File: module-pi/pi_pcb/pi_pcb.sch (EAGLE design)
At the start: 14 parts, among them K1 PIN20X2, X1 SSW-114-02-G-S, X2 SSW-114-02-G-S, X3 SSW-114-02-G-S, X4 SSW-114-02-G-S

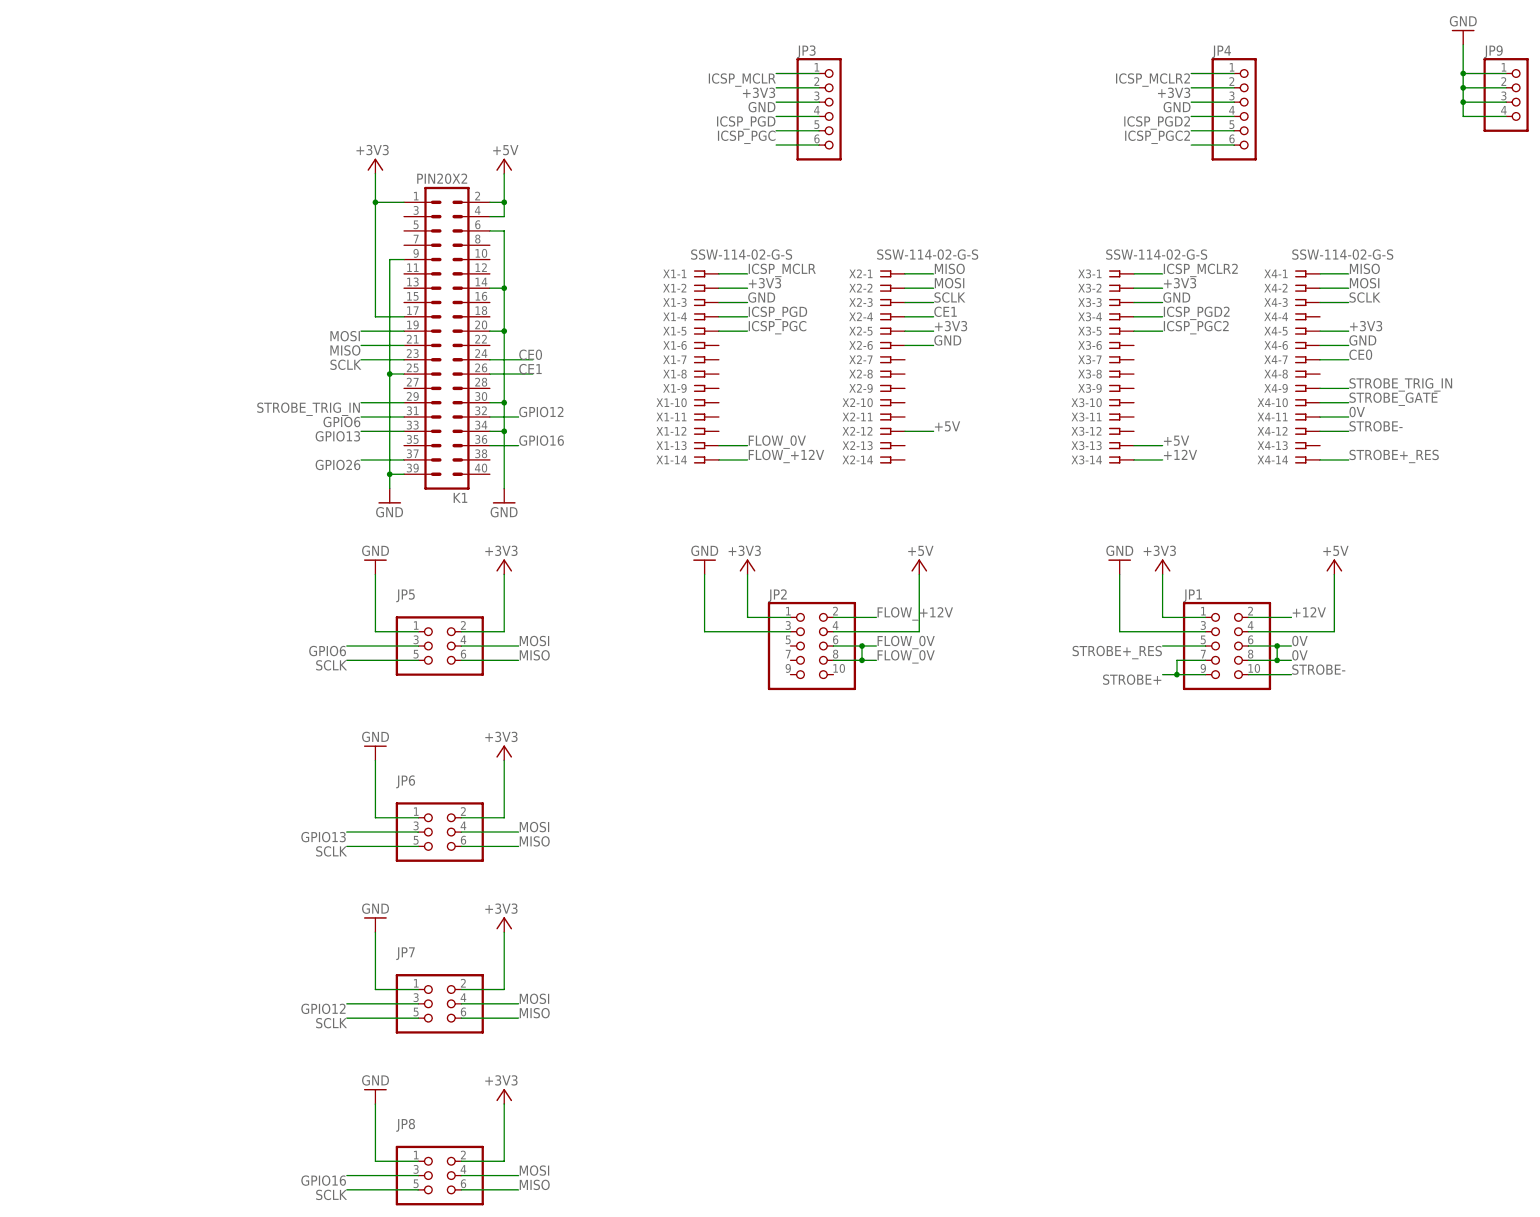
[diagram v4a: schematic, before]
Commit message: External strobe trigger added.  Text and boxes added.
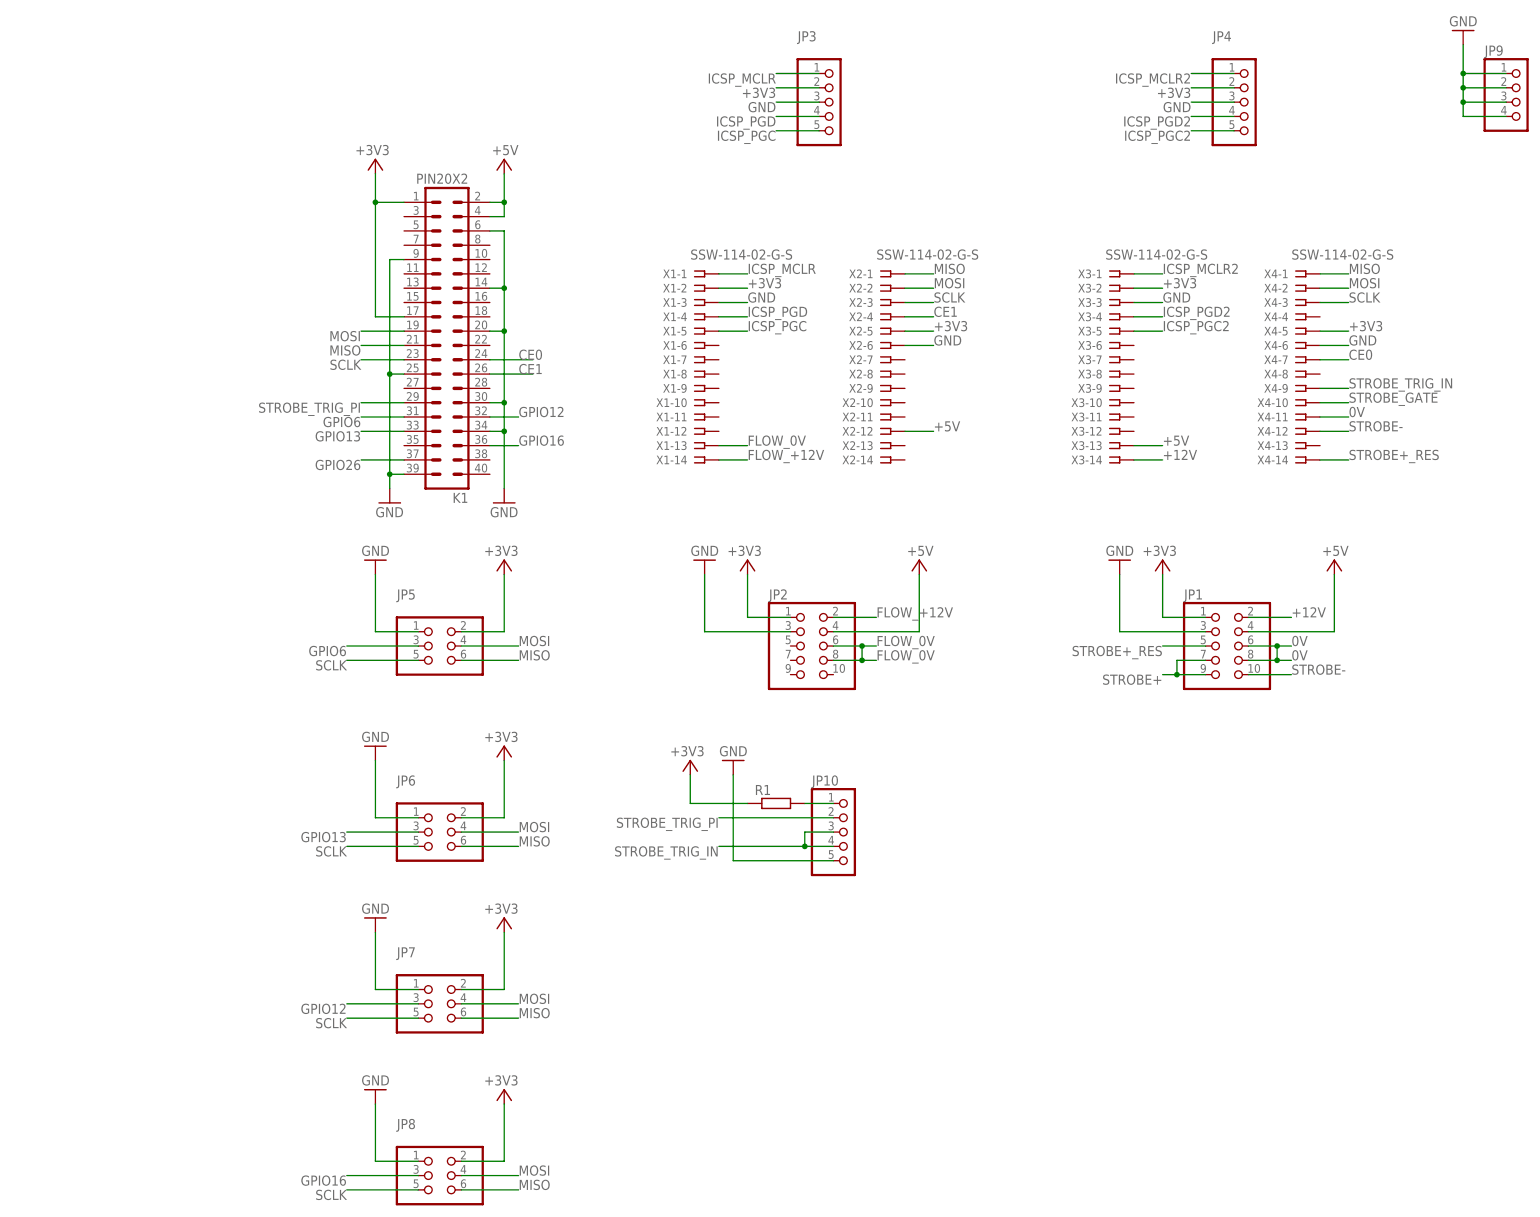
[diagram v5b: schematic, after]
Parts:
- added JP10: (no value), pinhead:PINHD-1X5
- added R1: (no value), rcl:R-EU_R1206
- JP3, JP4: device pinhead:PINHD-1X6 -> pinhead:PINHD-1X5
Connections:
- removed net N$6: JP4.6
- new net STROBE_TRIG_PI: JP10.2, K1.29
- net +3V3: now also R1.1
- net GND: now also JP10.5
- net N$1: now also JP10.1, R1.2; no longer JP3.6
- net STROBE_TRIG_IN: now also JP10.3, JP10.4; no longer K1.29

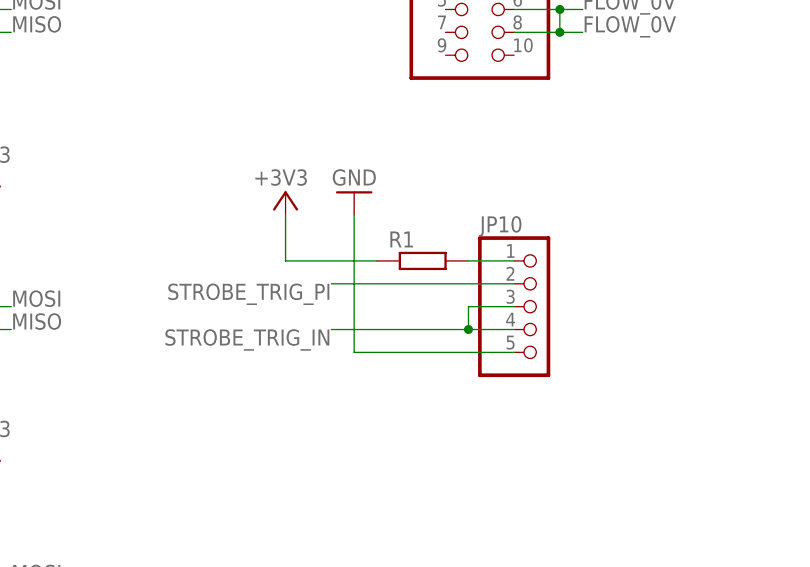
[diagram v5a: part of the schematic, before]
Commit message: Get and set sample holder power limit.
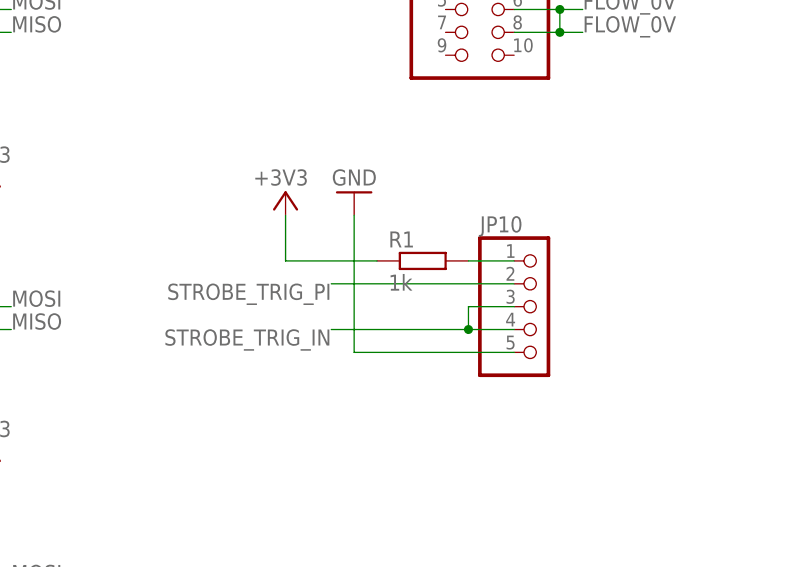
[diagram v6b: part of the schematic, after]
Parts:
- R1: value (none) -> 1k
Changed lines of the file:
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@@
 <?xml version="1.0" encoding="utf-8"?>
 <!DOCTYPE eagle SYSTEM "eagle.dtd">
-<eagle version="9.5.1">
+<eagle version="9.5.2">
 <drawing>
 <settings>
@@
 <grid distance="0.1" unitdist="inch" unit="inch" style="lines" multiple="1" display="no" altdistance="0.01" altunitdist="inch" altunit="inch"/>
 <layers>
-<layer number="1" name="Top" color="4" fill="1" visible="yes" active="no"/>
-<layer number="2" name="Route2" color="1" fill="3" visible="yes" active="no"/>
-<layer number="3" name="Route3" color="4" fill="3" visible="yes" active="no"/>
-<layer number="4" name="Route4" color="1" fill="4" visible="yes" active="no"/>
-<layer number="5" name="Route5" color="4" fill="4" visible="yes" active="no"/>
-<layer number="6" name="Route6" color="1" fill="8" visible="yes" active="no"/>
-<layer number="7" name="Route7" color="4" fill="8" visible="yes" active="no"/>
-<layer number="8" name="Route8" color="1" fill="2" visible="yes" active="no"/>
-<layer number="9" name="Route9" color="4" fill="2" visible="yes" active="no"/>
-<layer number="10" name="Route10" color="1" fill="7" visible="yes" active="no"/>
-<layer number="11" name="Route11" color="4" fill="7" visible="yes" active="no"/>
-<layer number="12" name="Route12" color="1" fill="5" visible="yes" active="no"/>
-<layer number="13" name="Route13" color="4" fill="5" visible="yes" active="no"/>
-<layer number="14" name="Route14" color="1" fill="6" visible="yes" active="no"/>
-<layer number="15" name="Route15" color="4" fill="6" visible="yes" active="no"/>
-<layer number="16" name="Bottom" color="1" fill="1" visible="yes" active="no"/>
-<layer number="17" name="Pads" color="2" fill="1" visible="yes" active="no"/>
-<layer number="18" name="Vias" color="2" fill="1" visible="yes" active="no"/>
-<layer number="19" name="Unrouted" color="6" fill="1" visible="yes" active="no"/>
-<layer number="20" name="Dimension" color="15" fill="1" visible="yes" active="no"/>
-<layer number="21" name="tPlace" color="7" fill="1" visible="yes" active="no"/>
-<layer number="22" name="bPlace" color="7" fill="1" visible="yes" active="no"/>
-<layer number="23" name="tOrigins" color="15" fill="1" visible="yes" active="no"/>
-<layer number="24" name="bOrigins" color="15" fill="1" visible="yes" active="no"/>
-<layer number="25" name="tNames" color="7" fill="1" visible="yes" active="no"/>
-<layer number="26" name="bNames" color="7" fill="1" visible="yes" active="no"/>
-<layer number="27" name="tValues" color="7" fill="1" visible="yes" active="no"/>
-<layer number="28" name="bValues" color="7" fill="1" visible="yes" active="no"/>
+<layer number="1" name="Top" color="4" fill="1" visible="no" active="no"/>
+<layer number="2" name="Route2" color="1" fill="3" visible="no" active="no"/>
+<layer number="3" name="Route3" color="4" fill="3" visible="no" active="no"/>
+<layer number="4" name="Route4" color="1" fill="4" visible="no" active="no"/>
+<layer number="5" name="Route5" color="4" fill="4" visible="no" active="no"/>
+<layer number="6" name="Route6" color="1" fill="8" visible="no" active="no"/>
+<layer number="7" name="Route7" color="4" fill="8" visible="no" active="no"/>
+<layer number="8" name="Route8" color="1" fill="2" visible="no" active="no"/>
+<layer number="9" name="Route9" color="4" fill="2" visible="no" active="no"/>
+<layer number="10" name="Route10" color="1" fill="7" visible="no" active="no"/>
+<layer number="11" name="Route11" color="4" fill="7" visible="no" active="no"/>
+<layer number="12" name="Route12" color="1" fill="5" visible="no" active="no"/>
+<layer number="13" name="Route13" color="4" fill="5" visible="no" active="no"/>
+<layer number="14" name="Route14" color="1" fill="6" visible="no" active="no"/>
+<layer number="15" name="Route15" color="4" fill="6" visible="no" active="no"/>
+<layer number="16" name="Bottom" color="1" fill="1" visible="no" active="no"/>
+<layer number="17" name="Pads" color="2" fill="1" visible="no" active="no"/>
+<layer number="18" name="Vias" color="2" fill="1" visible="no" active="no"/>
+<layer number="19" name="Unrouted" color="6" fill="1" visible="no" active="no"/>
+<layer number="20" name="Dimension" color="15" fill="1" visible="no" active="no"/>
+<layer number="21" name="tPlace" color="7" fill="1" visible="no" active="no"/>
+<layer number="22" name="bPlace" color="7" fill="1" visible="no" active="no"/>
+<layer number="23" name="tOrigins" color="15" fill="1" visible="no" active="no"/>
+<layer number="24" name="bOrigins" color="15" fill="1" visible="no" active="no"/>
+<layer number="25" name="tNames" color="7" fill="1" visible="no" active="no"/>
+<layer number="26" name="bNames" color="7" fill="1" visible="no" active="no"/>
+<layer number="27" name="tValues" color="7" fill="1" visible="no" active="no"/>
+<layer number="28" name="bValues" color="7" fill="1" visible="no" active="no"/>
 <layer number="29" name="tStop" color="7" fill="3" visible="no" active="no"/>
 <layer number="30" name="bStop" color="7" fill="6" visible="no" active="no"/>
@@
 <layer number="35" name="tGlue" color="7" fill="4" visible="no" active="no"/>
 <layer number="36" name="bGlue" color="7" fill="5" visible="no" active="no"/>
-<layer number="37" name="tTest" color="7" fill="1" visible="yes" active="no"/>
-<layer number="38" name="bTest" color="7" fill="1" visible="yes" active="no"/>
+<layer number="37" name="tTest" color="7" fill="1" visible="no" active="no"/>
+<layer number="38" name="bTest" color="7" fill="1" visible="no" active="no"/>
 <layer number="39" name="tKeepout" color="4" fill="11" visible="no" active="no"/>
 <layer number="40" name="bKeepout" color="1" fill="11" visible="no" active="no"/>
@@
 <layer number="44" name="Drills" color="7" fill="1" visible="no" active="no"/>
 <layer number="45" name="Holes" color="7" fill="1" visible="no" active="no"/>
-<layer number="46" name="Milling" color="3" fill="1" visible="yes" active="no"/>
-<layer number="47" name="Measures" color="7" fill="1" visible="yes" active="no"/>
-<layer number="48" name="Document" color="7" fill="1" visible="yes" active="no"/>
-<layer number="49" name="Reference" color="7" fill="1" visible="yes" active="no"/>
-<layer number="50" name="dxf" color="7" fill="1" visible="yes" active="no"/>
-<layer number="51" name="tDocu" color="7" fill="1" visible="yes" active="no"/>
-<layer number="52" name="bDocu" color="7" fill="1" visible="yes" active="no"/>
-<layer number="53" name="tGND_GNDA" color="7" fill="1" visible="yes" active="no"/>
-<layer number="54" name="bGND_GNDA" color="7" fill="1" visible="yes" active="no"/>
-<layer number="56" name="wert" color="7" fill="1" visible="yes" active="no"/>
+<layer number="46" name="Milling" color="3" fill="1" visible="no" active="no"/>
+<layer number="47" name="Measures" color="7" fill="1" visible="no" active="no"/>
+<layer number="48" name="Document" color="7" fill="1" visible="no" active="no"/>
+<layer number="49" name="Reference" color="7" fill="1" visible="no" active="no"/>
+<layer number="50" name="dxf" color="7" fill="1" visible="no" active="no"/>
+<layer number="51" name="tDocu" color="7" fill="1" visible="no" active="no"/>
+<layer number="52" name="bDocu" color="7" fill="1" visible="no" active="no"/>
+<layer number="53" name="tGND_GNDA" color="7" fill="1" visible="no" active="no"/>
+<layer number="54" name="bGND_GNDA" color="7" fill="1" visible="no" active="no"/>
+<layer number="56" name="wert" color="7" fill="1" visible="no" active="no"/>
 <layer number="90" name="Modules" color="5" fill="1" visible="yes" active="yes"/>
 <layer number="91" name="Nets" color="2" fill="1" visible="yes" active="yes"/>
@@
 <part name="+3V2" library="supply1" deviceset="+3V3" device=""/>
 <part name="GND2" library="supply1" deviceset="GND" device=""/>
-<part name="R1" library="rcl" library_urn="urn:adsk.eagle:library:334" deviceset="R-EU_" device="R1206" package3d_urn="urn:adsk.eagle:package:23540/2"/>
+<part name="R1" library="rcl" library_urn="urn:adsk.eagle:library:334" deviceset="R-EU_" device="R1206" package3d_urn="urn:adsk.eagle:package:23540/2" value="1k"/>
 </parts>
 <sheets>
